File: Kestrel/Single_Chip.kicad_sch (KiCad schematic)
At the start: 46 parts, among them Q2 BC817, Q3 BC807, Q4 BC817, Q6 SI2301, SW2 SKRKAGE020, U3 SY6918

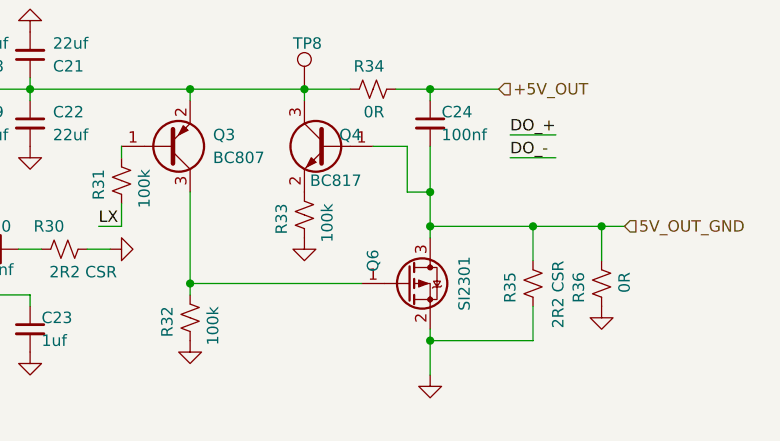
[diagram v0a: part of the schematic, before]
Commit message: values updated in the tp circuit
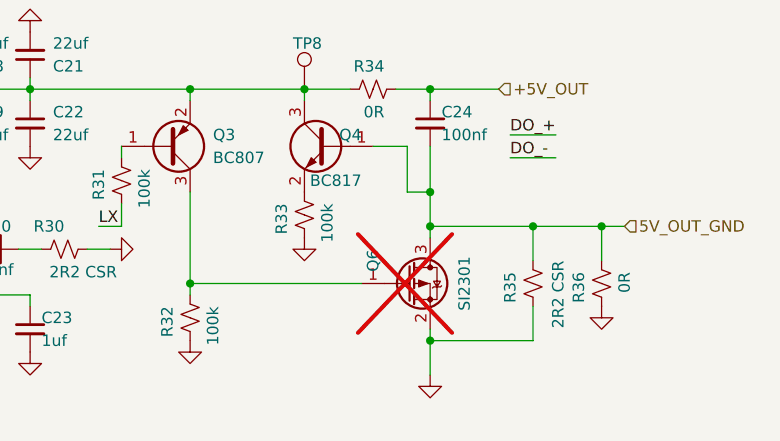
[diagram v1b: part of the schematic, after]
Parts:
- Q6: now not fitted
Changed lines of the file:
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@@
 		(in_bom yes)
 		(on_board yes)
-		(dnp no)
+		(dnp yes)
 		(property "Reference" "Q6"
 			(at 198.12 106.68 90)

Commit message: schematic updated
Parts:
- C24, Q2, Q3, Q4, R16, R23, R25, R26, R28, R29, R31, R32, R33, R35: now not fitted
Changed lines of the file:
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@@
 	(wire
 		(pts
-			(xy 213.36 92.71) (xy 218.44 92.71)
-		)
-		(stroke
-			(width 0)
-			(type default)
-		)
-	)
-	(wire
-		(pts
 			(xy 127 77.47) (xy 133.35 77.47)
 		)
@@
 	(wire
 		(pts
-			(xy 213.36 95.25) (xy 218.44 95.25)
-		)
-		(stroke
-			(width 0)
-			(type default)
-		)
-	)
-	(wire
-		(pts
 			(xy 132.08 88.9) (xy 132.08 87.63)
 		)
@@
 		)
 	)
-	(label "DO_+"
-		(at 213.36 92.71 0)
-		(effects
-			(font
-				(size 1.27 1.27)
-			)
-			(justify left bottom)
-		)
-	)
 	(label "LX"
 		(at 151.13 105.41 0)
@@
 		)
 	)
-	(label "DO_-"
-		(at 213.36 95.25 0)
-		(effects
-			(font
-				(size 1.27 1.27)
-			)
-			(justify left bottom)
-		)
-	)
 	(label "SYS"
 		(at 74.93 109.22 0)
@@
 		(in_bom yes)
 		(on_board yes)
-		(dnp no)
+		(dnp yes)
 		(property "Reference" "R35"
 			(at 213.36 107.95 90)
@@
 		(in_bom yes)
 		(on_board yes)
-		(dnp no)
+		(dnp yes)
 		(property "Reference" "R31"
 			(at 167.64 96.52 90)
@@
 		(in_bom yes)
 		(on_board yes)
-		(dnp no)
+		(dnp yes)
 		(property "Reference" "R26"
 			(at 128.27 88.9 0)
@@
 		(in_bom yes)
 		(on_board yes)
-		(dnp no)
+		(dnp yes)
 		(property "Reference" "Q4"
 			(at 196.85 92.71 0)
@@
 		(in_bom yes)
 		(on_board yes)
-		(dnp no)
+		(dnp yes)
 		(property "Reference" "R29"
 			(at 142.24 105.41 90)
@@
 		(in_bom yes)
 		(on_board yes)
-		(dnp no)
+		(dnp yes)
 		(property "Reference" "Q2"
 			(at 143.51 95.25 0)
@@
 		(in_bom yes)
 		(on_board yes)
-		(dnp no)
+		(dnp yes)
 		(property "Reference" "C24"
 			(at 205.74 90.17 0)
@@
 		(in_bom no)
 		(on_board yes)
-		(dnp no)
+		(dnp yes)
 		(property "Reference" "R28"
 			(at 142.24 99.06 90)
@@
 		(in_bom yes)
 		(on_board yes)
-		(dnp no)
+		(dnp yes)
 		(property "Reference" "R23"
 			(at 124.46 80.01 90)
@@
 		(in_bom yes)
 		(on_board yes)
-		(dnp no)
+		(dnp yes)
 		(property "Reference" "R33"
 			(at 187.96 100.33 90)
@@
 		(in_bom yes)
 		(on_board yes)
-		(dnp no)
+		(dnp yes)
 		(property "Reference" "R25"
 			(at 120.65 76.2 90)
@@
 		(in_bom yes)
 		(on_board yes)
-		(dnp no)
+		(dnp yes)
 		(property "Reference" "R32"
 			(at 175.26 111.76 90)
@@
 		(in_bom yes)
 		(on_board yes)
-		(dnp no)
+		(dnp yes)
 		(property "Reference" "R16"
 			(at 74.93 100.33 90)
@@
 		(in_bom yes)
 		(on_board yes)
-		(dnp no)
+		(dnp yes)
 		(fields_autoplaced yes)
 		(property "Reference" "Q3"
